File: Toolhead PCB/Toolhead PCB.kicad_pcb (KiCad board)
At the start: 2 copper layers, 31.5 x 26.6 mm, 12 parts, among them J1 PicoA, J2 PicoB, J3 PicoC, J4 Heater, J5 Thermistor, J6 Heatbreak, J7 Part, J8 IR/ADXL, J9 µProbe

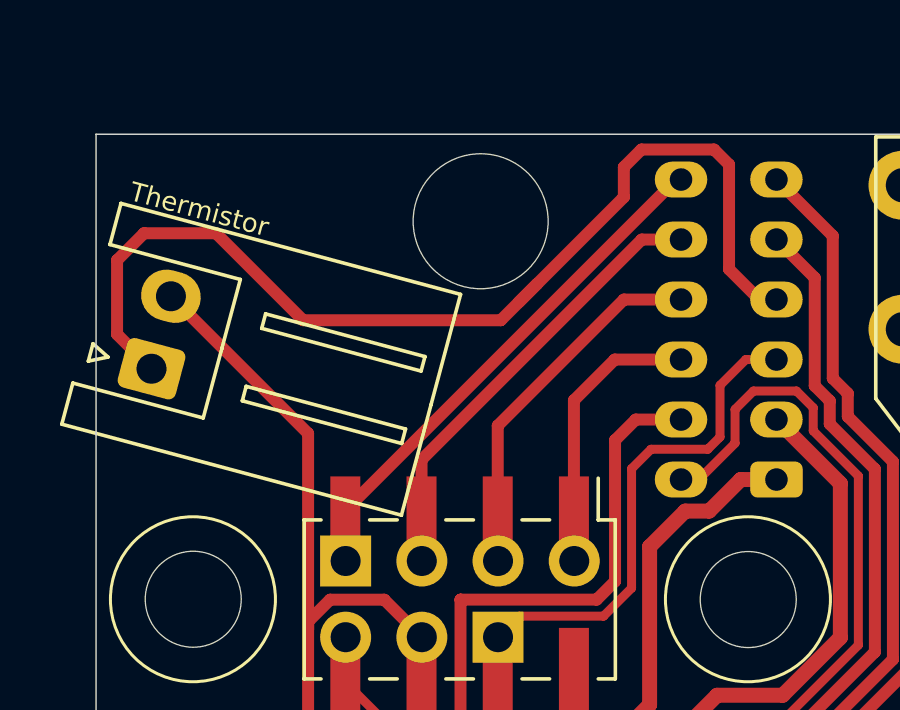
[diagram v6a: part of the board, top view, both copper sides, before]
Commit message: Schematic more closely matches traces. Updated PicoB and PicoC wiring harnesses: flagged as non populated and deleted silkscreen. Removed pins from Muon 3D IR Bed Probe with ADXL345. Moved traces from PicoB to IR/ADXL so they might be easier to mill.
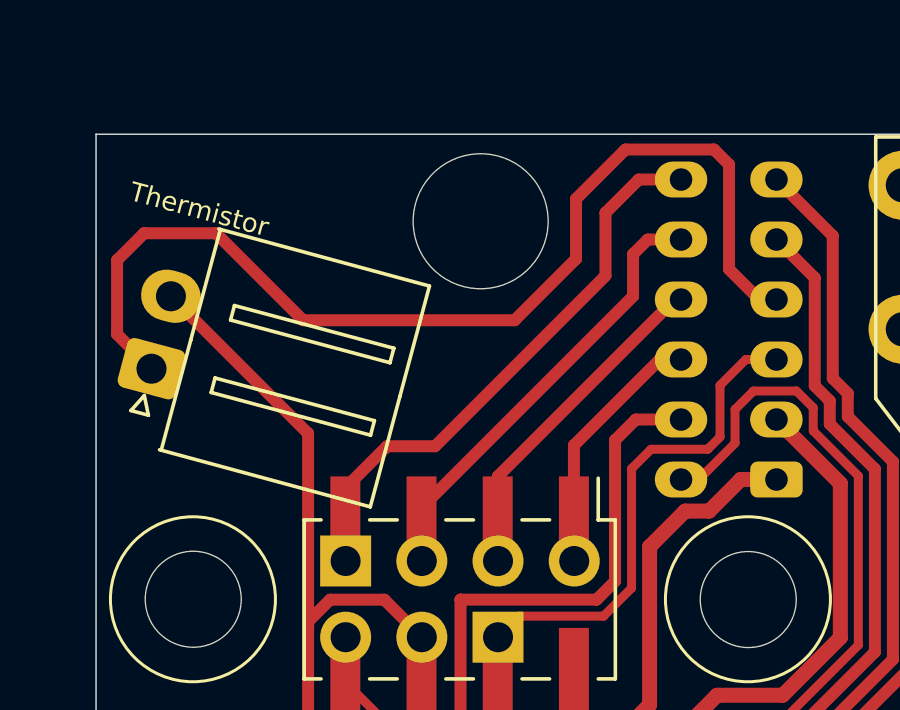
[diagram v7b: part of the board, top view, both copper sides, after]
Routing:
- net /MO: track 11.1 -> 10.1 mm
- net /CS: track 17.1 -> 18.0 mm
- net /SC: track 8.27 -> 7.39 mm

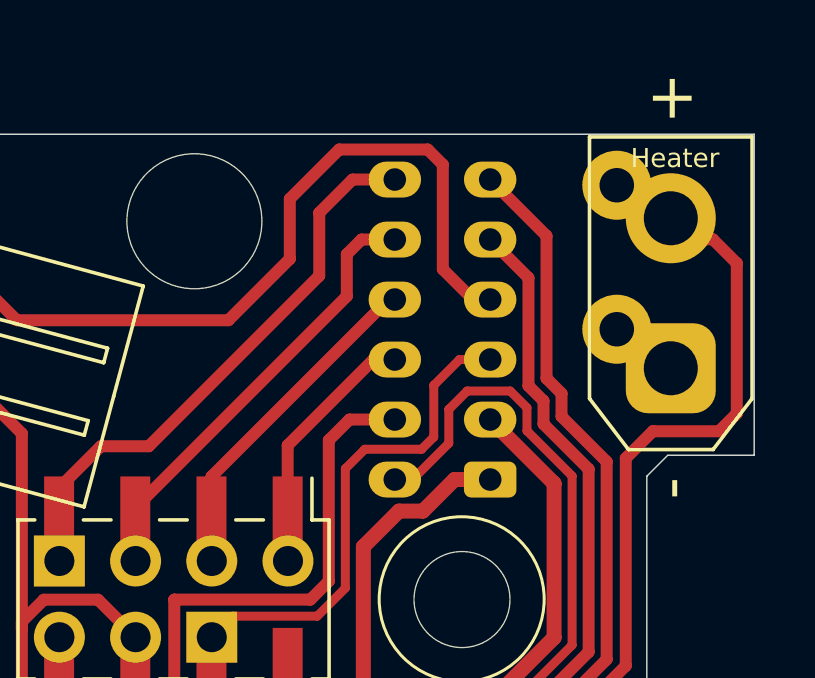
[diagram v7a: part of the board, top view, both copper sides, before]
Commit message: The 0.75mm holes do not retain the Silicone 28AWG Ribbon Cable wires properly, so the Schematic and PCB use a new footprint `SolderWire-0.1sqmm_1x06_P2.0mm_D0.4mm_OD1mm.kicad_mod` which has the same pitch and pads as the JST PH but the holes 0.75mm → 0.5mm.
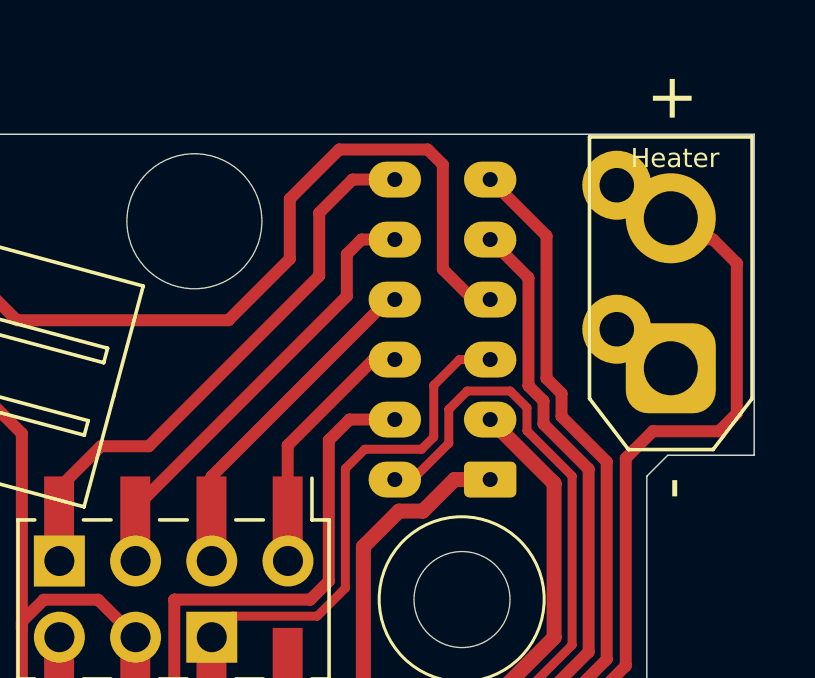
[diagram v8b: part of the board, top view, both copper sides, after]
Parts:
- J2, J3: footprint Connector_JST:JST_PH_B6B-PH-K_1x06_P2.00mm_Vertical -> Positron V3:SolderWire-0.1sqmm_1x06_P2.0mm_D0.4mm_OD1mm
